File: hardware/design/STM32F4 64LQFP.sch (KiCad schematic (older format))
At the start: 18 parts, among them P2 CONN_01X05, U1 STM32F40X_LQFP64, X2 8MHz 10ppm

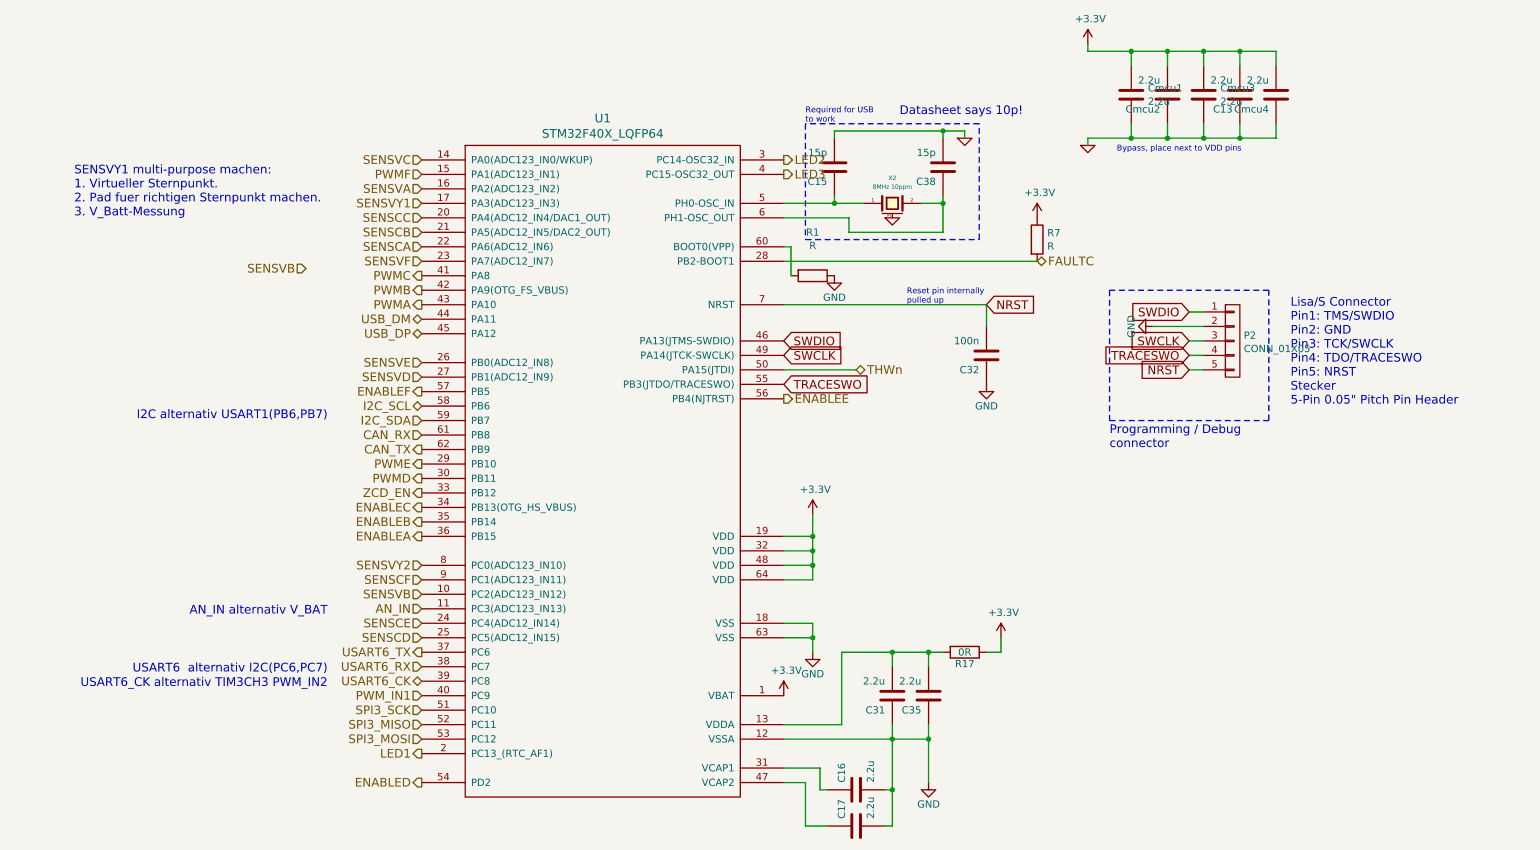
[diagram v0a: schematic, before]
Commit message: Six-phase power stage.
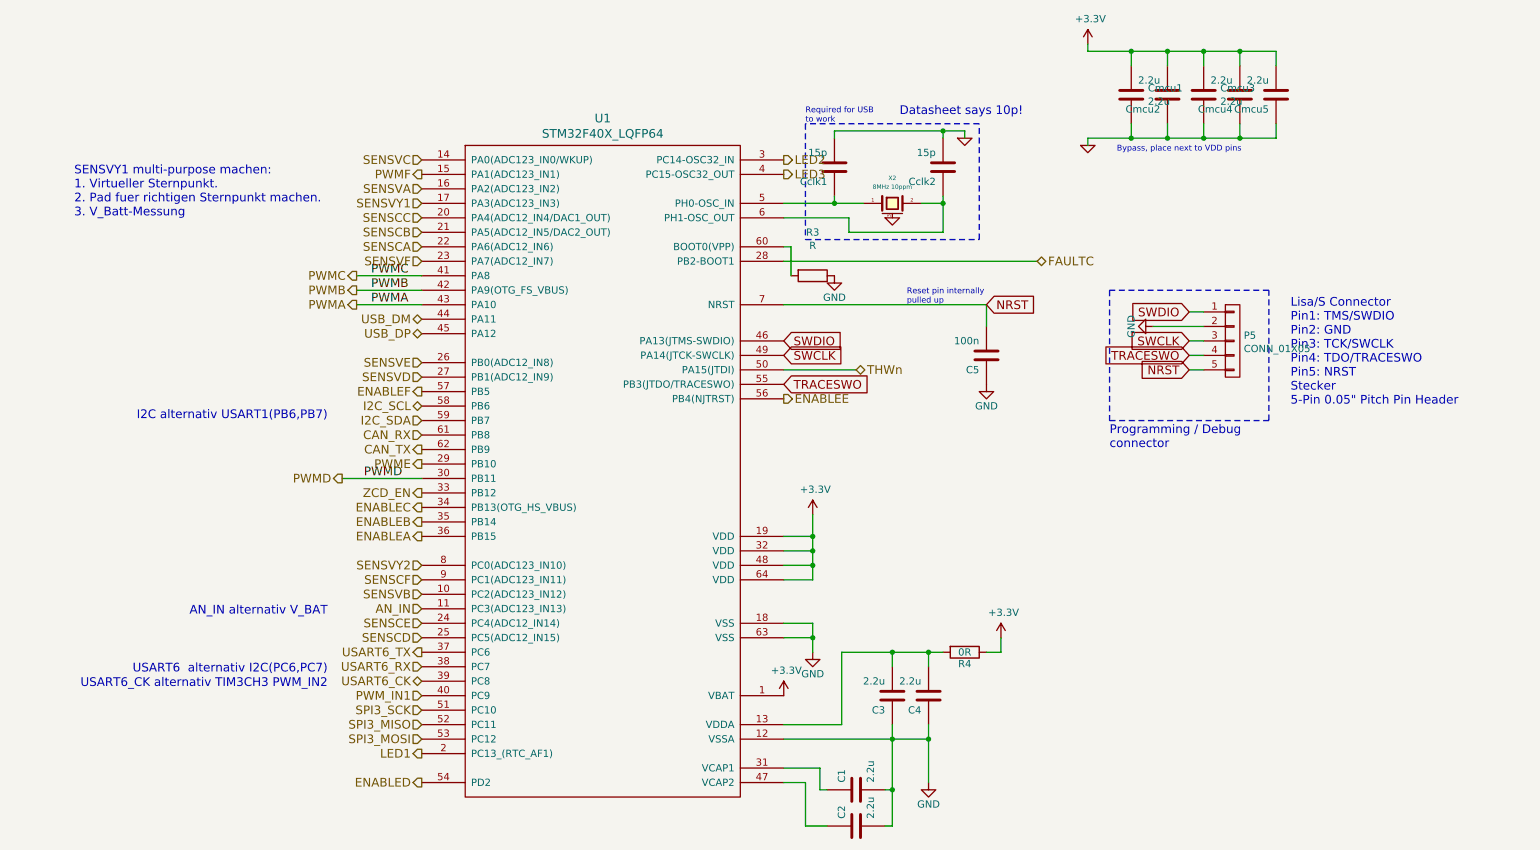
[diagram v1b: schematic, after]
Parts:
- removed R7: R, Resistors_SMD:R_0603, symbol R
- renumbered C16 to C1, C17 to C2, C31 to C3, C35 to C4, C32 to C5, C15 to Cclk1, C38 to Cclk2, C13 to Cmcu4, Cmcu4 to Cmcu5, P2 to P5, R1 to R3, R17 to R4
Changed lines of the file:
@@
 $Descr A4 11693 8268
 encoding utf-8
-Sheet 3 6
+Sheet 3 12
 Title "3-Phase Universal Driver"
 Date "2015-08-27"
@@
 $EndDescr
 $Comp
-L C-RESCUE-BLDC_4 C17
+L C-RESCUE-BLDC_4 C2
 U 1 1 53F757AE
 P 7500 6350
-F 0 "C17" H 7550 6450 50  0000 L CNN
+F 0 "C2" H 7550 6450 50  0000 L CNN
 F 1 "2.2u" H 7550 6250 50  0000 L CNN
 F 2 "Capacitors_SMD:C_0603" H 7500 6350 60  0001 C CNN
@@
 $EndComp
 $Comp
-L C-RESCUE-BLDC_4 C16
+L C-RESCUE-BLDC_4 C1
 U 1 1 53F757B5
 P 7500 6100
-F 0 "C16" H 7550 6200 50  0000 L CNN
+F 0 "C1" H 7550 6200 50  0000 L CNN
 F 1 "2.2u" H 7550 6000 50  0000 L CNN
 F 2 "Capacitors_SMD:C_0603" H 7500 6100 60  0001 C CNN
@@
 $EndComp
 $Comp
-L C-RESCUE-BLDC_4 C15
+L C-RESCUE-BLDC_4 Cclk1
 U 1 1 53F757DB
 P 7350 1800
-F 0 "C15" H 7400 1900 50  0000 L CNN
+F 0 "Cclk1" H 7400 1900 50  0000 L CNN
 F 1 "15p" H 7400 1700 50  0000 L CNN
 F 2 "Capacitors_SMD:C_0402" H 7350 1800 60  0001 C CNN
@@
 $EndComp
 $Comp
-L C-RESCUE-BLDC_4 C38
+L C-RESCUE-BLDC_4 Cclk2
 U 1 1 53F757E2
 P 8100 1800
-F 0 "C38" H 8150 1900 50  0000 L CNN
+F 0 "Cclk2" H 8150 1900 50  0000 L CNN
 F 1 "15p" H 8150 1700 50  0000 L CNN
 F 2 "Capacitors_SMD:C_0402" H 8100 1800 60  0001 C CNN
@@
 SWCLK
 $Comp
-L C-RESCUE-BLDC_4 C31
+L C-RESCUE-BLDC_4 C3
 U 1 1 53F757F8
 P 7750 5450
-F 0 "C31" H 7800 5550 50  0000 L CNN
+F 0 "C3" H 7800 5550 50  0000 L CNN
 F 1 "2.2u" H 7800 5350 50  0000 L CNN
 F 2 "Capacitors_SMD:C_0603" H 7750 5450 60  0001 C CNN
@@
 $EndComp
 $Comp
-L C-RESCUE-BLDC_4 C35
+L C-RESCUE-BLDC_4 C4
 U 1 1 53F757FF
 P 8000 5450
-F 0 "C35" H 8050 5550 50  0000 L CNN
+F 0 "C4" H 8050 5550 50  0000 L CNN
 F 1 "2.2u" H 8050 5350 50  0000 L CNN
 F 2 "Capacitors_SMD:C_0603" H 8000 5450 60  0001 C CNN
@@
 	7750 6350 7700 6350
 $Comp
-L C-RESCUE-BLDC_4 C32
+L C-RESCUE-BLDC_4 C5
 U 1 1 53F75896
 P 8400 3100
-F 0 "C32" H 8450 3200 50  0000 L CNN
+F 0 "C5" H 8450 3200 50  0000 L CNN
 F 1 "100n" H 8450 3000 50  0000 L CNN
 F 2 "Capacitors_SMD:C_0603" H 8400 3100 60  0001 C CNN
@@
 $EndComp
 $Comp
-L C-RESCUE-BLDC_4 Cmcu4
+L C-RESCUE-BLDC_4 Cmcu5
 U 1 1 53F77434
 P 10400 1300
-F 0 "Cmcu4" H 10450 1400 50  0000 L CNN
+F 0 "Cmcu5" H 10450 1400 50  0000 L CNN
 F 1 "2.2u" H 10450 1200 50  0000 L CNN
 F 2 "Capacitors_SMD:C_0603" H 10400 1300 60  0001 C CNN
@@
 $EndComp
 $Comp
-L GND-RESCUE-BLDC_4 #PWR27
+L GND-RESCUE-BLDC_4 #PWR26
 U 1 1 53F7743B
 P 9100 1650
-F 0 "#PWR27" H 9100 1650 30  0001 C CNN
+F 0 "#PWR26" H 9100 1650 30  0001 C CNN
 F 1 "GND" H 9100 1580 30  0001 C CNN
 F 2 "" H 9100 1650 60  0001 C CNN
@@
 $EndComp
 $Comp
-L C-RESCUE-BLDC_4 C13
+L C-RESCUE-BLDC_4 Cmcu4
 U 1 1 53F7744E
 P 10150 1300
-F 0 "C13" H 10200 1400 50  0000 L CNN
+F 0 "Cmcu4" H 10200 1400 50  0000 L CNN
 F 1 "2.2u" H 10200 1200 50  0000 L CNN
 F 2 "Capacitors_SMD:C_0603" H 10150 1300 60  0001 C CNN
@@
 Text HLabel 4500 3850 0    60   Output ~ 0
 PWME
-Text HLabel 4500 3950 0    60   Output ~ 0
+Text HLabel 3950 3950 0    60   Output ~ 0
 PWMD
 Text HLabel 4500 4550 0    60   Input ~ 0
@@
 Text HLabel 4500 5250 0    60   Input ~ 0
 USART6_RX
-Text HLabel 4500 2550 0    60   Output ~ 0
+Text HLabel 4050 2550 0    60   Output ~ 0
 PWMC
-Text HLabel 4500 2650 0    60   Output ~ 0
+Text HLabel 4050 2650 0    60   Output ~ 0
 PWMB
-Text HLabel 4500 2750 0    60   Output ~ 0
+Text HLabel 4050 2750 0    60   Output ~ 0
 PWMA
 Text HLabel 4500 1750 0    60   Input ~ 0
 SENSVC
-Text HLabel 3700 2500 0    60   Input ~ 0
-SENSVB
 Text HLabel 4500 1950 0    60   Input ~ 0
 SENSVA
@@
 $EndComp
 $Comp
-L GND #PWR28
+L GND #PWR27
 U 1 1 55E72286
 P 9550 2900
-F 0 "#PWR28" H 9550 2650 50  0001 C CNN
+F 0 "#PWR27" H 9550 2650 50  0001 C CNN
 F 1 "GND" H 9550 2750 50  0000 C CNN
 F 2 "" H 9550 2900 60  0000 C CNN
@@
 	7400 5150 7400 5650
 $Comp
-L R R17
+L R R4
 U 1 1 55E738BB
 P 8250 5150
-F 0 "R17" V 8330 5150 50  0000 C CNN
+F 0 "R4" V 8330 5150 50  0000 C CNN
 F 1 "0R" V 8250 5150 50  0000 C CNN
 F 2 "Resistors_SMD:R_0603_HandSoldering" V 8180 5150 30  0001 C CNN
@@
 	1    0    0    -1
 $EndComp
-$Comp
-L R R7
-U 1 1 56A5C8AD
-P 8750 2300
-F 0 "R7" H 8820 2346 50  0000 L CNN
-F 1 "R" H 8820 2254 50  0000 L CNN
-F 2 "Resistors_SMD:R_0603" V 8680 2300 50  0001 C CNN
-F 3 "" H 8750 2300 50  0000 C CNN
-	1    8750 2300
-	1    0    0    -1
-$EndComp
-$Comp
-L +3.3V #PWR25
-U 1 1 56A5C94A
-P 8750 2150
-F 0 "#PWR25" H 8750 2000 50  0001 C CNN
-F 1 "+3.3V" H 8768 2324 50  0000 C CNN
-F 2 "" H 8750 2150 50  0000 C CNN
-F 3 "" H 8750 2150 50  0000 C CNN
-	1    8750 2150
-	1    0    0    -1
-$EndComp
 Text GLabel 9800 3100 0    60   Input ~ 0
 TRACESWO
@@
 TRACESWO
 $Comp
-L CONN_01X05 P2
+L CONN_01X05 P5
 U 1 1 56A6A68D
 P 10100 3000
-F 0 "P2" H 10177 3038 50  0000 L CNN
+F 0 "P5" H 10177 3038 50  0000 L CNN
 F 1 "CONN_01X05" H 10177 2946 50  0000 L CNN
 F 2 "Socket_Strips:Socket_Strip_Straight_1x05" H 10100 3000 50  0001 C CNN
@@
 Wire Wire Line
 	9800 3200 9900 3200
-Text HLabel 4500 1850 0    60   Input ~ 0
+Text HLabel 4500 1850 0    60   Output ~ 0
 PWMF
 Wire Wire Line
@@
 ENABLED
 $Comp
-L R R1
+L R R3
 U 1 1 56A6E871
 P 7200 2550
-F 0 "R1" V 6900 2550 50  0000 C CNN
+F 0 "R3" V 6900 2550 50  0000 C CNN
 F 1 "R" V 6992 2550 50  0000 C CNN
 F 2 "Resistors_SMD:R_0603_HandSoldering" V 7084 2550 50  0001 C CNN
@@
 	7050 2350 7050 2550
 $Comp
-L +3.3V #PWR26
+L +3.3V #PWR25
 U 1 1 56A683FD
 P 9100 950
-F 0 "#PWR26" H 9100 800 50  0001 C CNN
+F 0 "#PWR25" H 9100 800 50  0001 C CNN
 F 1 "+3.3V" H 9118 1124 50  0000 C CNN
 F 2 "" H 9100 950 50  0000 C CNN
@@
 Text Notes 7800 1450 0    60   ~ 0
 Datasheet says 10p!
+Wire Wire Line
+	4050 2750 4500 2750
+Text Label 4150 2750 0    60   ~ 0
+PWMA
+Wire Wire Line
+	4050 2650 4500 2650
+Text Label 4150 2650 0    60   ~ 0
+PWMB
+Wire Wire Line
+	4500 2550 4050 2550
+Text Label 4150 2550 0    60   ~ 0
+PWMC
+Wire Wire Line
+	3950 3950 4500 3950
+Text Label 4100 3950 0    60   ~ 0
+PWMD
 $EndSCHEMATC

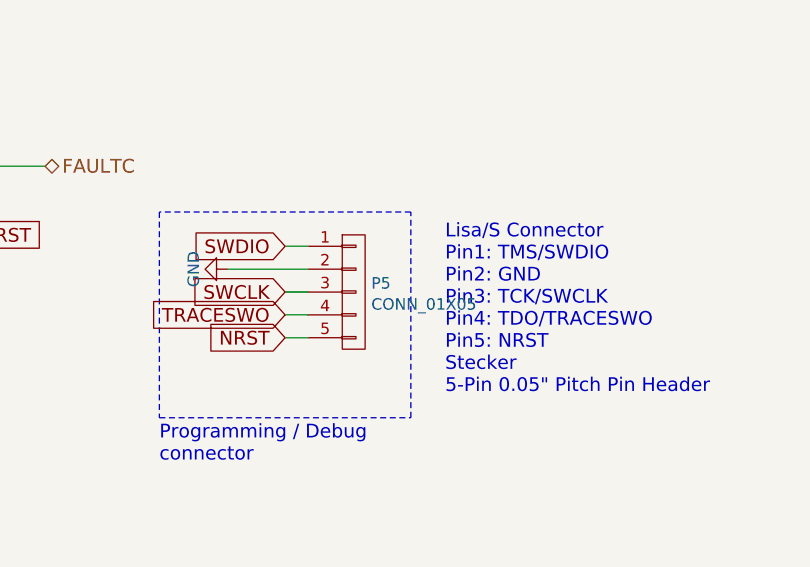
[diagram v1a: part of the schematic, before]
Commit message: TODO: Routing of the DSBL-signals.
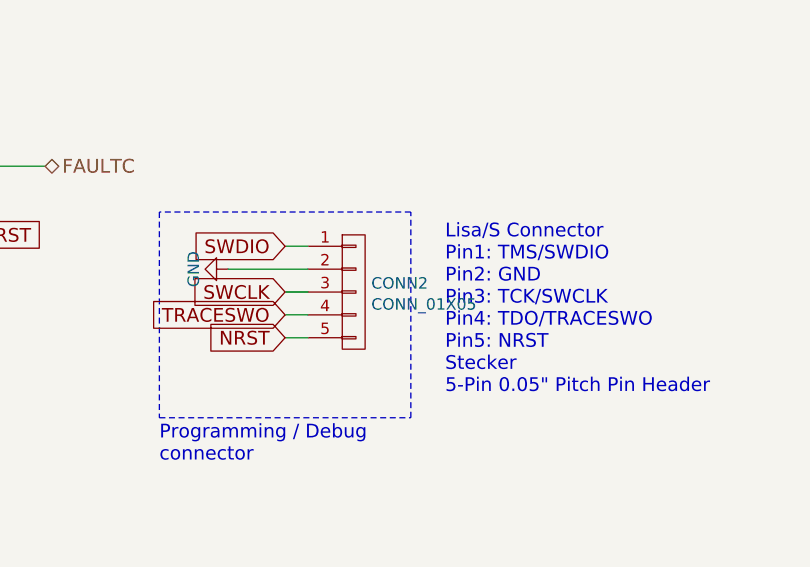
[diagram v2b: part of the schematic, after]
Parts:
- renumbered P5 to CONN2
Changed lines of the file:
@@
 $Descr A4 11693 8268
 encoding utf-8
-Sheet 3 12
+Sheet 3 11
 Title "3-Phase Universal Driver"
 Date "2015-08-27"
@@
 TRACESWO
 $Comp
-L CONN_01X05 P5
+L CONN_01X05 CONN2
 U 1 1 56A6A68D
 P 10100 3000
-F 0 "P5" H 10177 3038 50  0000 L CNN
+F 0 "CONN2" H 10177 3038 50  0000 L CNN
 F 1 "CONN_01X05" H 10177 2946 50  0000 L CNN
 F 2 "Socket_Strips:Socket_Strip_Straight_1x05" H 10100 3000 50  0001 C CNN

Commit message: TODO: Find appropriate routing to CPU
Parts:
- R3: value R -> R/DNP; footprint Resistors_SMD:R_0603_HandSoldering -> Resistors_SMD:R_0402
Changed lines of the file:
@@
 U 1 1 56A6E871
 P 7200 2550
-F 0 "R3" V 6900 2550 50  0000 C CNN
-F 1 "R" V 6992 2550 50  0000 C CNN
-F 2 "Resistors_SMD:R_0603_HandSoldering" V 7084 2550 50  0001 C CNN
+F 0 "R3" V 6992 2550 50  0000 C CNN
+F 1 "R/DNP" V 7084 2550 50  0000 C CNN
+F 2 "Resistors_SMD:R_0402" V 7084 2550 50  0001 C CNN
 F 3 "" H 7200 2550 50  0000 C CNN
 	1    7200 2550

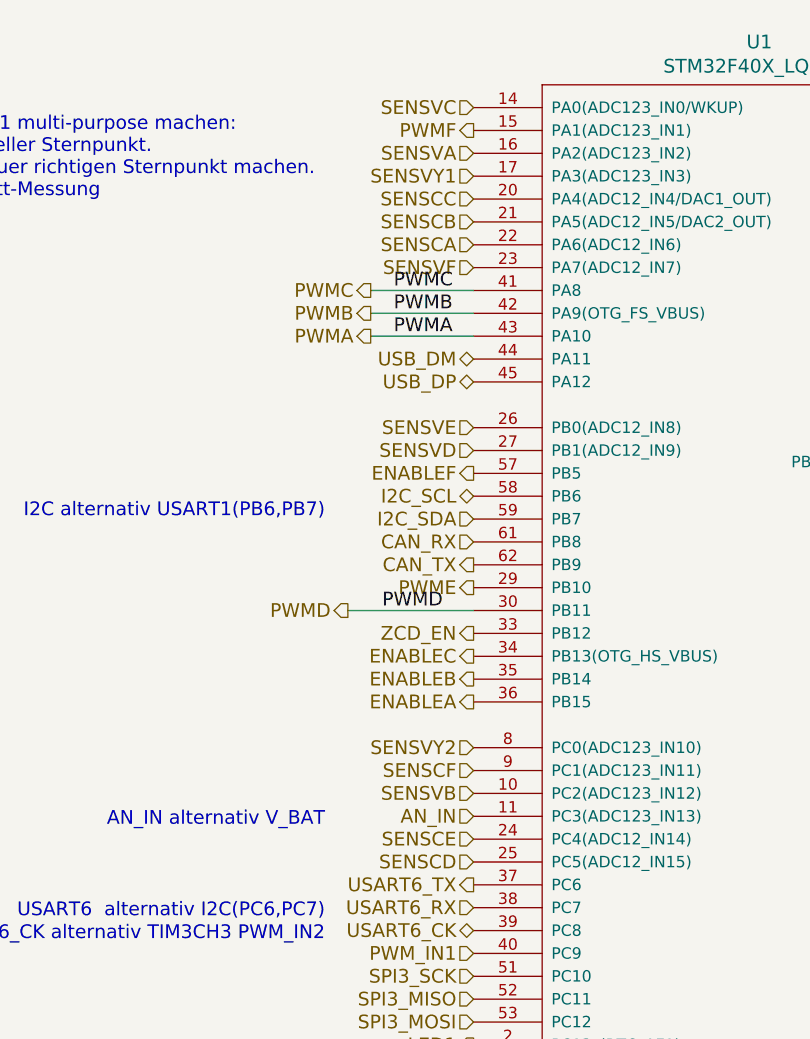
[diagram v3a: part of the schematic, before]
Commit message: New analog pin configuration for better rounting
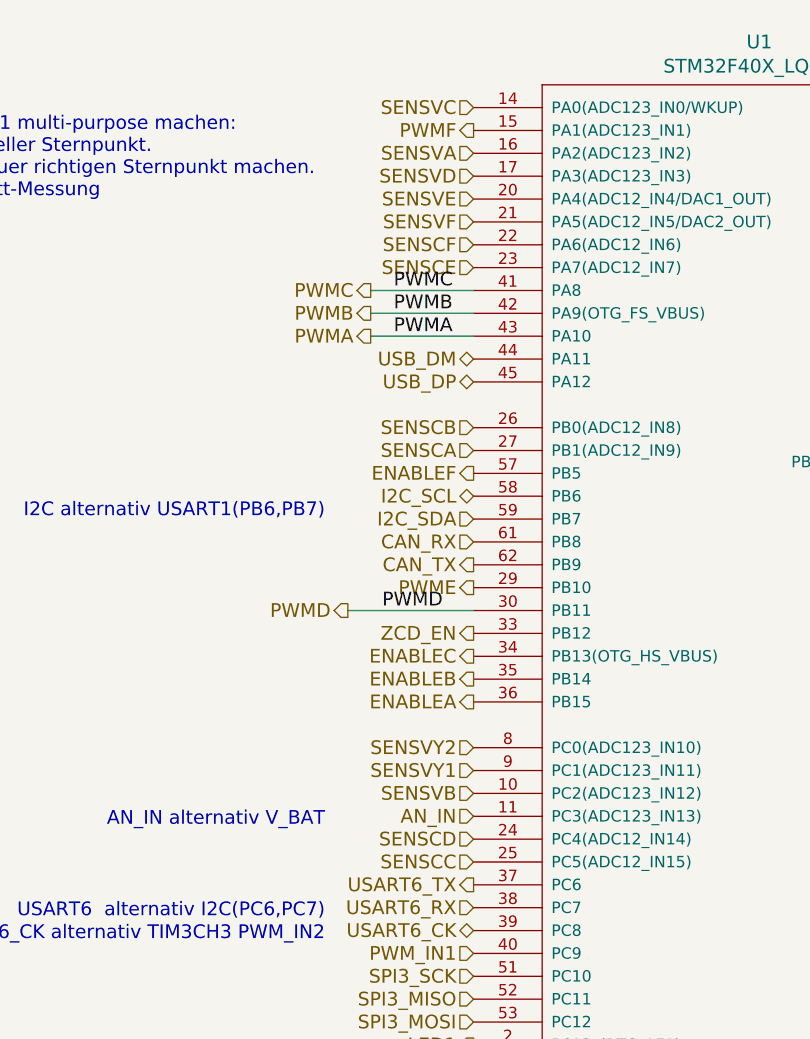
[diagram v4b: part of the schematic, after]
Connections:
- net SENSCA: now also U1.27 (PB1(ADC12_IN9)); no longer U1.22 (PA6(ADC12_IN6))
- net SENSCB: now also U1.26 (PB0(ADC12_IN8)); no longer U1.21 (PA5(ADC12_IN5/DAC2_OUT))
- net SENSCC: now also U1.25 (PC5(ADC12_IN15)); no longer U1.20 (PA4(ADC12_IN4/DAC1_OUT))
- net SENSCD: now also U1.24 (PC4(ADC12_IN14)); no longer U1.25 (PC5(ADC12_IN15))
- net SENSCE: now also U1.23 (PA7(ADC12_IN7)); no longer U1.24 (PC4(ADC12_IN14))
- net SENSCF: now also U1.22 (PA6(ADC12_IN6)); no longer U1.9 (PC1(ADC123_IN11))
- net SENSVD: now also U1.17 (PA3(ADC123_IN3)); no longer U1.27 (PB1(ADC12_IN9))
- net SENSVE: now also U1.20 (PA4(ADC12_IN4/DAC1_OUT)); no longer U1.26 (PB0(ADC12_IN8))
- net SENSVF: now also U1.21 (PA5(ADC12_IN5/DAC2_OUT)); no longer U1.23 (PA7(ADC12_IN7))
- net SENSVY1: now also U1.9 (PC1(ADC123_IN11)); no longer U1.17 (PA3(ADC123_IN3))
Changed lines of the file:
@@
 Text HLabel 4500 4350 0    60   Output ~ 0
 ENABLEA
-Text HLabel 4500 5050 0    60   Input ~ 0
+Text HLabel 4500 4950 0    60   Input ~ 0
 SENSCD
 Text HLabel 4500 5150 0    60   Output ~ 0
@@
 Text HLabel 4500 1950 0    60   Input ~ 0
 SENSVA
-Text HLabel 4500 2350 0    60   Input ~ 0
+Text HLabel 4500 3250 0    60   Input ~ 0
 SENSCA
-Text HLabel 4500 2250 0    60   Input ~ 0
+Text HLabel 4500 3150 0    60   Input ~ 0
 SENSCB
 Text HLabel 4500 4850 0    60   Input ~ 0
@@
 Text HLabel 4500 3750 0    60   Output ~ 0
 CAN_TX
-Text HLabel 4500 4950 0    60   Input ~ 0
+Text HLabel 4500 2450 0    60   Input ~ 0
 SENSCE
 $Comp
@@
 	1    0    0    -1
 $EndComp
-Text HLabel 4500 4650 0    60   Input ~ 0
+Text HLabel 4500 2350 0    60   Input ~ 0
 SENSCF
-Text HLabel 4500 2050 0    60   Input ~ 0
+Text HLabel 4500 4650 0    60   Input ~ 0
 SENSVY1
-Text HLabel 4500 2150 0    60   Input ~ 0
+Text HLabel 4500 5050 0    60   Input ~ 0
 SENSCC
 Text HLabel 4500 3450 0    60   3State ~ 0
@@
 Text Notes 10500 3450 0    60   ~ 0
 Lisa/S Connector\nPin1: TMS/SWDIO\nPin2: GND\nPin3: TCK/SWCLK\nPin4: TDO/TRACESWO\nPin5: NRST\nStecker\n5-Pin 0.05" Pitch Pin Header
-Text HLabel 4500 3150 0    60   Input ~ 0
+Text HLabel 4500 2150 0    60   Input ~ 0
 SENSVE
-Text HLabel 4500 3250 0    60   Input ~ 0
+Text HLabel 4500 2050 0    60   Input ~ 0
 SENSVD
-Text HLabel 4500 2450 0    60   Input ~ 0
+Text HLabel 4500 2250 0    60   Input ~ 0
 SENSVF
 Text Notes 2100 2150 0    60   ~ 0
